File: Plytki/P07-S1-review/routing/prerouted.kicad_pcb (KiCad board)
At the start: 2 copper layers, 106.5 x 100 mm, 156 parts, among them J1 VMOTOR, J2 MOD B+/B-, J3 MOD M+/M-, J4 TEST, J5 J_MOD, K1 G2RL-1-E DC5, Q1 AO3400A, Q2 MMBT3904, U1 INA240A2, U10 74LVC125AD, U11 74LVC14AD, U12 SN74HC08D, U13 SN74HC08D, U14 SN74HC08D, U15 SN74HC74D, U16 74AHCT125D, U17 74LVC2G17, U18 MCP1702-3302E/TO, U2 MCP1525-I/TO, U3 MCP6022-I/SN, U4 MCP6022-I/SN, U5 TLV1702AIDR, U6 MCP3201-BI/P, U7 74LVC125AD, U8 MCP120-300DI/TO, U9 MCP120-450DI/TO

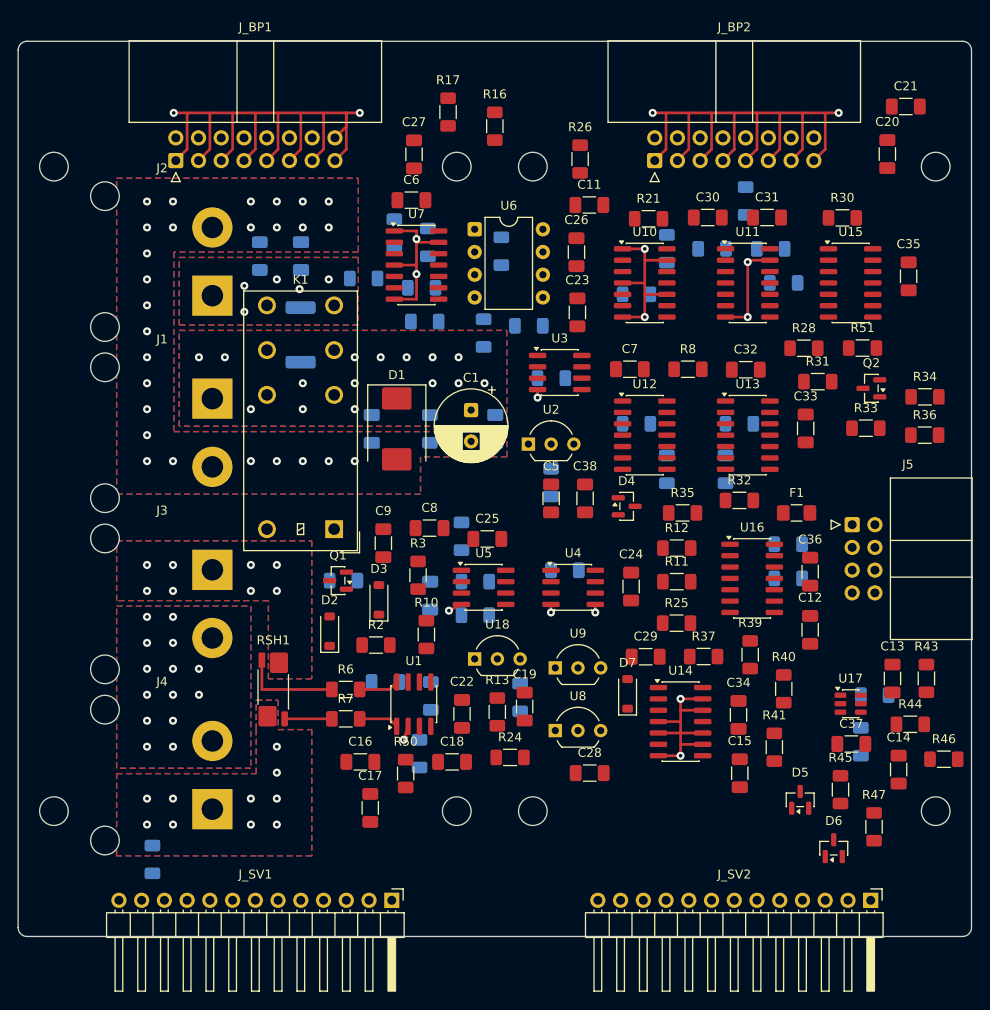
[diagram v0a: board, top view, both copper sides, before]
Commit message: P07 S1: uproszczenia 6.10 (jedna listwa serwisowa, MOTOR_PERMIT / PWM_OUT bez odbiornika Ioff, diagnostyka IS bez Schmitta, rozmieszczenie przy złączach) — ERC 0, 16/16, S1 27/27; trasowanie nadal NIEDOMKNIĘTE (13 przerw sygnałowych), stan w README
Co-Authored-By: Claude Opus 5.5 <noreply@anthropic.com>
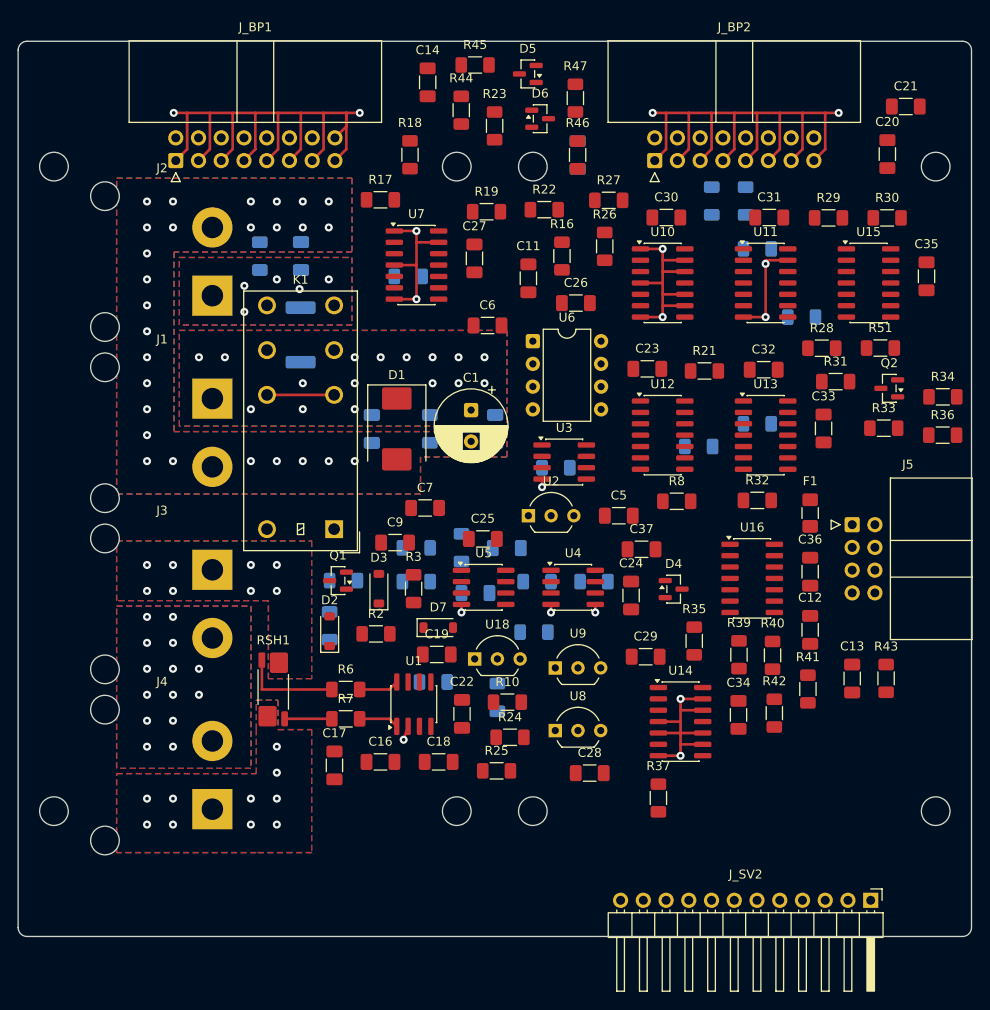
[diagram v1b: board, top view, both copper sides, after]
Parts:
- removed C38: 100n, Capacitor_SMD:C_1206_3216Metric_Pad1.33x1.80mm_HandSolder
- removed J_SV1: J_SV1 SERWIS 1x13, Connector_PinHeader_2.54mm:PinHeader_1x13_P2.54mm_Horizontal
- removed R48, R49: 100R, Resistor_SMD:R_1206_3216Metric_Pad1.30x1.75mm_HandSolder
- removed R61: 4K7, Resistor_SMD:R_1206_3216Metric_Pad1.30x1.75mm_HandSolder
- removed R62, R63, R64, R65, R66, R67, R68, R69, R70, R71: 1K, Resistor_SMD:R_1206_3216Metric_Pad1.30x1.75mm_HandSolder
- removed U17: 74LVC2G17, Package_TO_SOT_SMD:SOT-23-6
- C14: value 10n -> 100n
- C15: value 10n -> 100n; moved to B.Cu
- C8, R11, R12, R13, R50: moved to B.Cu
- J_SV2: value J_SV2 SERWIS 1x13 -> J_SV2 SERWIS 1x12; footprint Connector_PinHeader_2.54mm:PinHeader_1x13_P2.54mm_Horizontal -> Connector_PinHeader_2.54mm:PinHeader_1x12_P2.54mm_Horizontal
- R18, R19, R22, R23, R27, R29, R42: moved to F.Cu
- R44, R46: value 100K -> 4K7
- R52, R53, R54, R55, R56, R57: value 10K -> 1K
- R58, R59: value 4K7 -> 1K
- R60: value 4K7 -> 10K
- moved C14 93.1 mm to (45.8, 4.59), turned to 90 degrees
- moved R45 90.7 mm to (51.0, 2.65), turned to 0 degrees
- moved R47 88.0 mm to (62.2, 6.35), turned to 90 degrees
- moved D6 87.8 mm to (58.3, 8.65), turned to 0 degrees
- moved D5 86.6 mm to (56.9, 3.65), turned to 180 degrees
- moved R44 85.0 mm to (49.5, 7.70), turned to 90 degrees
- moved R46 78.9 mm to (62.5, 12.7), turned to 90 degrees
- moved C15 71.4 mm to (62.5, 12.7)
- moved R52 65.5 mm to (81.3, 17.8)
- moved R57 51.6 mm to (82.6, 23.2)
- moved R53 41.2 mm to (46.4, 71.6)
- moved R59 39.8 mm to (77.5, 17.8), turned to -90 degrees
- moved R56 38.7 mm to (87.5, 30.8)
- moved C37 32.0 mm to (69.6, 56.8), turned to 0 degrees
- moved C7 27.6 mm to (45.5, 52.1), turned to 180 degrees
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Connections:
- net NO_TRIP renamed /LOGIKA/NO_TRIP
- net RAILS_OK renamed /LOGIKA/RAILS_OK
- net T_EGR_P1 renamed /MOC/T_EGR_P1
- C10 pad 1: OC_LOW -> /ANA/OC_LOW
- C11 pad 1: ADC_AIN -> /DIG/ADC_AIN
- C14 pad 1: /MODUL/ISR_DIV -> ENA_DIAG
- C15 pad 1: /MODUL/ISL_DIV -> ENB_DIAG
- C37 pad 1: 3V3_IO -> 3V3A_P07
- C4 pad 1: MOD_BP -> /MOC/MOD_BP
- D5 pad 3: /MODUL/ISR_DIV -> ENA_DIAG
- D6 pad 3: /MODUL/ISL_DIV -> ENB_DIAG
- J2 pad 1: MOD_BP -> /MOC/MOD_BP
- J_SV2 pad 10: /SERWIS/SRV_OC_GOOD -> GND
- J_SV2 pad 11: /SERWIS/SRV_NO_TRIP -> /SERWIS/SRV_I_T_OUT
- J_SV2 pad 12: /SERWIS/SRV_DRIVE_EN -> GND
- J_SV2 pad 5: /SERWIS/SRV_3V3_IO -> /SERWIS/SRV_KPWR_COIL_LOW
- J_SV2 pad 6: /SERWIS/SRV_5V_MOD -> /SERWIS/SRV_SAFE_OK
- J_SV2 pad 7: GND -> /SERWIS/SRV_OC_LOCAL_N
- J_SV2 pad 8: /SERWIS/SRV_RAILS_OK -> /SERWIS/SRV_OC_GOOD
- J_SV2 pad 9: /SERWIS/SRV_OC_LOCAL_N -> /SERWIS/SRV_DRIVE_OK
- K1 pad 14: MOD_BP -> /MOC/MOD_BP
- R11 pad 1: OC_HIGH -> /ANA/OC_HIGH
- R13 pad 1: REF_BUF -> /ANA/REF_BUF
- R13 pad 2: OC_LOW -> /ANA/OC_LOW
- R14 pad 1: OC_LOW -> /ANA/OC_LOW
- R16 pad 2: ADC_AIN -> /DIG/ADC_AIN
- R4 pad 2: MOD_BP -> /MOC/MOD_BP
- R44 pad 2: /MODUL/ISR_DIV -> ENA_DIAG
- R45 pad 1: /MODUL/ISR_DIV -> ENA_DIAG
- R46 pad 2: /MODUL/ISL_DIV -> ENB_DIAG
- R47 pad 1: /MODUL/ISL_DIV -> ENB_DIAG
- R5 pad 1: MOD_BP -> /MOC/MOD_BP
- R52 pad 1: I_T_OUT -> 5V_SYS
- R52 pad 2: /SERWIS/SRV_I_T_OUT -> /SERWIS/SRV_5V_SYS
- R53 pad 1: ADC_AIN -> 5VA_P07
- R53 pad 2: /SERWIS/SRV_ADC_AIN -> /SERWIS/SRV_5VA_P07
- R54 pad 1: REF_BUF -> 3V3A_P07
- R54 pad 2: /SERWIS/SRV_REF_BUF -> /SERWIS/SRV_3V3A_P07
- R55 pad 1: REF25 -> KPWR_COIL_LOW
- R55 pad 2: /SERWIS/SRV_REF25 -> /SERWIS/SRV_KPWR_COIL_LOW
- R56 pad 1: OC_HIGH -> SAFE_OK
- R56 pad 2: /SERWIS/SRV_OC_HIGH -> /SERWIS/SRV_SAFE_OK
- R57 pad 1: OC_LOW -> OC_LOCAL_N
- R57 pad 2: /SERWIS/SRV_OC_LOW -> /SERWIS/SRV_OC_LOCAL_N
- R58 pad 1: VMOTOR -> OC_GOOD
- R58 pad 2: /SERWIS/SRV_VMOTOR -> /SERWIS/SRV_OC_GOOD
- R59 pad 1: MOD_BP -> DRIVE_OK
- R59 pad 2: /SERWIS/SRV_MOD_BP -> /SERWIS/SRV_DRIVE_OK
- R60 pad 1: KPWR_COIL_LOW -> I_T_OUT
- R60 pad 2: /SERWIS/SRV_KPWR_COIL_LOW -> /SERWIS/SRV_I_T_OUT
- U1 pad 3: REF_BUF -> /ANA/REF_BUF
- U1 pad 7: REF_BUF -> /ANA/REF_BUF
- U10 pad 11: /LOGIKA/PWM_P07 -> unconnected-(U10-4Y-Pad11)
- U10 pad 12: PWM_OUT -> GND
- U10 pad 8: /LOGIKA/PERMIT_P07 -> unconnected-(U10-3Y-Pad8)
- U10 pad 9: MOTOR_PERMIT -> GND
- U11 pad 3: /LOGIKA/PERMIT_P07 -> MOTOR_PERMIT
- U11 pad 8: /LOGIKA/SAFE_OK -> SAFE_OK
- U12 pad 9: /LOGIKA/PERMIT_P07 -> MOTOR_PERMIT
- U13 pad 2: /LOGIKA/SAFE_OK -> SAFE_OK
- U13 pad 9: /LOGIKA/PWM_P07 -> PWM_OUT
- U3 pad 6: REF_BUF -> /ANA/REF_BUF
- U3 pad 7: REF_BUF -> /ANA/REF_BUF
- U4 pad 1: OC_HIGH -> /ANA/OC_HIGH
- U4 pad 3: REF_BUF -> /ANA/REF_BUF
- U5 pad 2: OC_LOW -> /ANA/OC_LOW
- U5 pad 5: OC_HIGH -> /ANA/OC_HIGH
- U6 pad 2: ADC_AIN -> /DIG/ADC_AIN
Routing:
- net unconnected-(K1-NC-Pad12): track 0.00 -> 7.50 mm
- net GND: track 216.9 -> 221.2 mm
- net VMOTOR: vias 15 -> 16
- net MOD_BP: vias 5 -> 0
- net /MOC/MOD_BP: vias 0 -> 5
- added copper zone on B.Cu, net /MOC/MOD_BP
- added copper zone on F.Cu, net /MOC/MOD_BP
- removed copper zone on B.Cu, net MOD_BP
- removed copper zone on F.Cu, net MOD_BP
